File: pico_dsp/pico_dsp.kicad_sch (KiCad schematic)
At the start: 81 parts, among them J1 HDR_20, J2 HDR_20, J3 SJ3-35082B-TR, J4 SJ3-35082B-TR, J5 SJ3-35082B-TR, J7 SJ3-35082B-TR, SW1 RotaryEncoder_Switch, SW2 RotaryEncoder_Switch, U1 PCM5102A, U2 PCM1802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

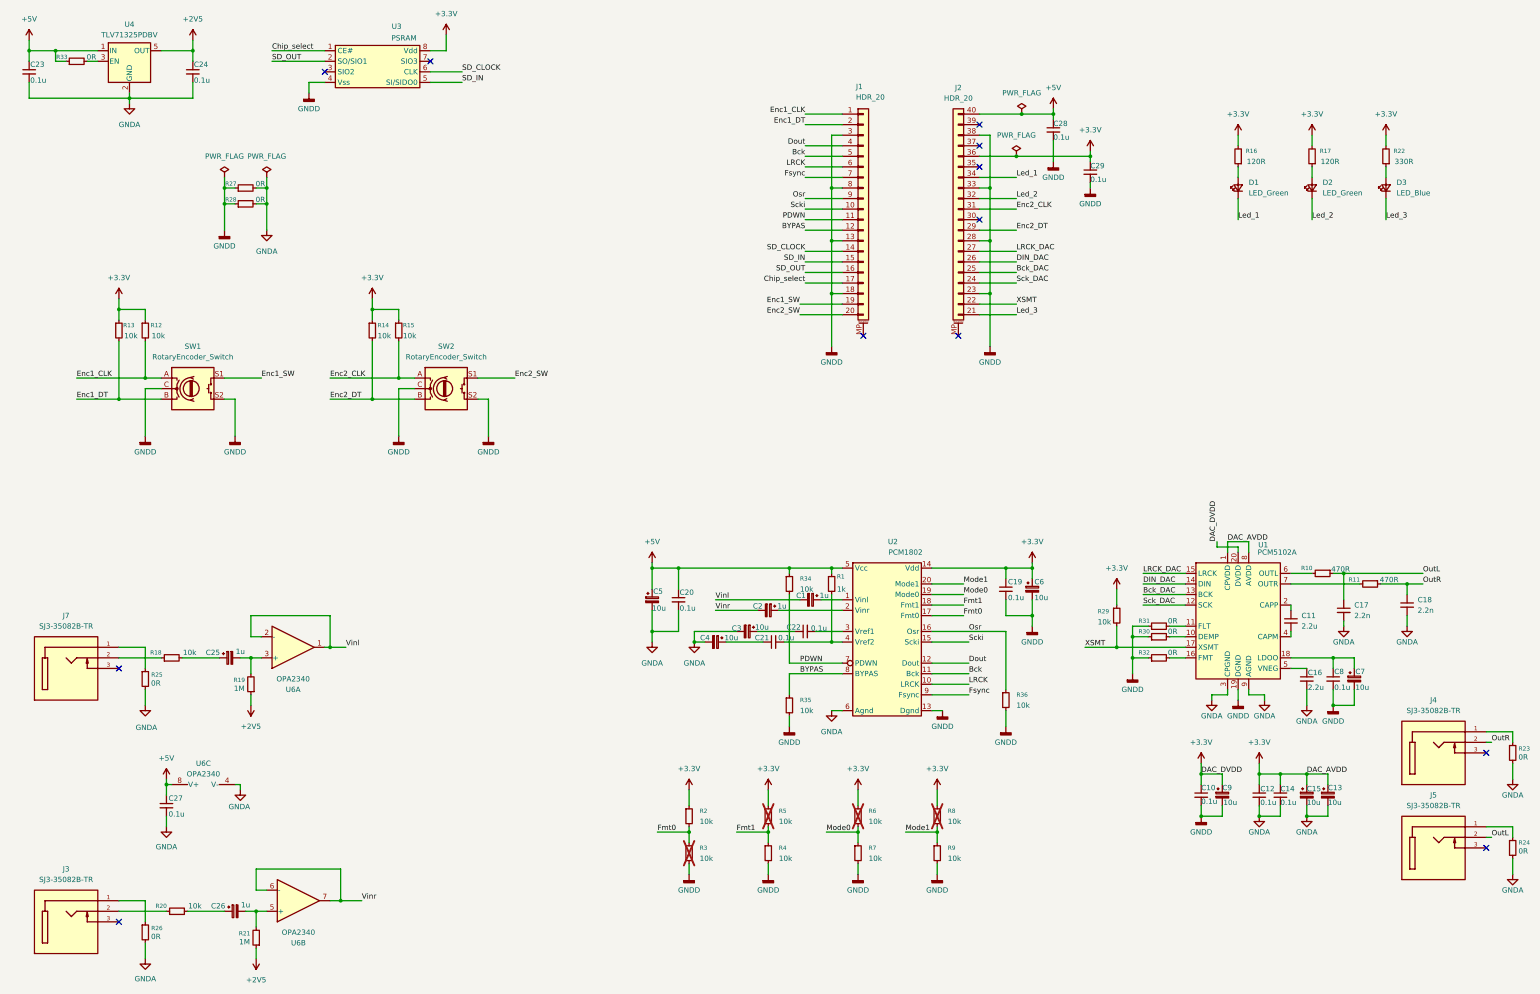
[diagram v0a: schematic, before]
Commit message: Added pads and updated pcb
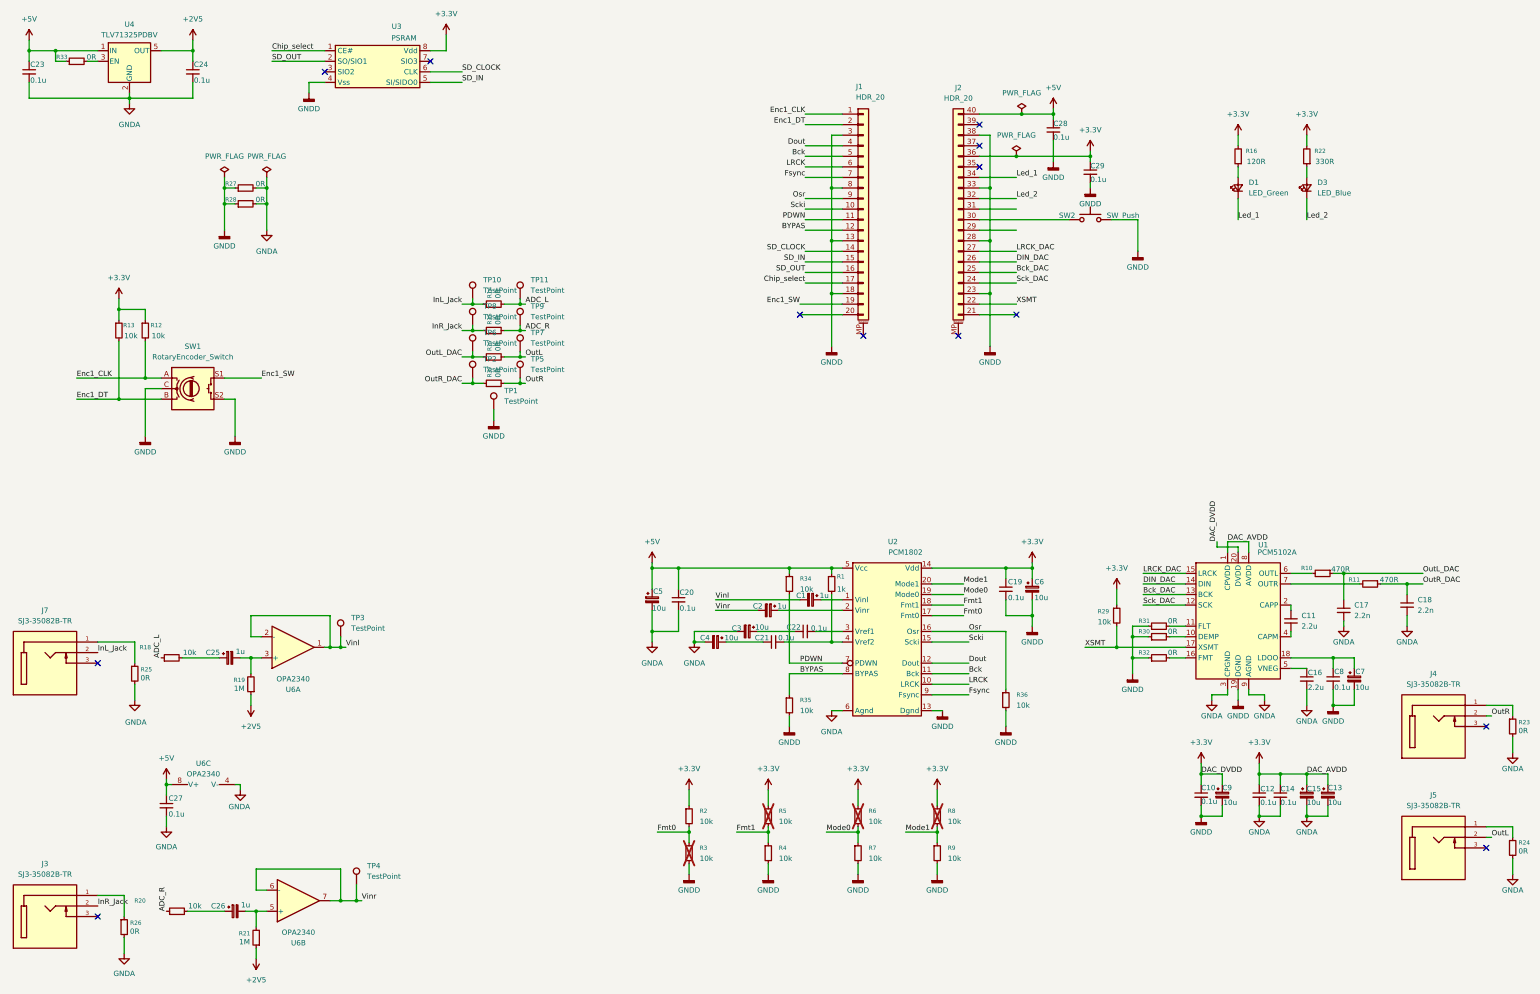
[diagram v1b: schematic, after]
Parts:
- removed D2: LED_Green, LED_SMD:LED_0603_1608Metric, symbol Device:LED_Small
- removed SW2: RotaryEncoder_Switch, Rotary_Encoder:RotaryEncoder_Bourns_Vertical_PEC12R-3x17F-Sxxxx, symbol Device:RotaryEncoder_Switch
- added R37: 0R, Resistor_SMD:R_0603_1608Metric, symbol Device:R_Small
- added SW2: SW_Push, Button_Switch_THT:SW_PUSH_6mm, symbol Switch:SW_Push
- added TP1, TP10, TP11, TP2, TP3, TP4, TP5, TP6, TP7, TP8, TP9: TestPoint, TestPoint:TestPoint_Pad_1.5x1.5mm, symbol Connector:TestPoint
- J3, J4, J5, J7: footprint SJ3-35082B-TR:SAMESKY_SJ3-35082B-TR -> Kicad-symbols:SAMESKY_SJ3-35082B-TR
- R14, R15: value 10k -> 0R
- R17: value 120R -> 0R
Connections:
- net +3.3V: no longer R14.1, R15.1, R17.2
- net GNDD: now also SW2.2, TP1.1
- net Led_2: now also D3.1 (K)
- net OutL: now also R17.2, TP7.1; no longer C17.1, R10.1
- net OutR: now also R37.2, TP5.1; no longer C18.1, R11.1
- net Vinl: now also TP3.1
- net Vinr: now also TP4.1
- net OutL_DAC: now reaches R17.1
- net OutL_DAC: now also C17.1, R10.1, TP6.1
- net at J2.30 (Pin_30): now also SW2.1
- net ADC_R: now reaches R20.1
- net ADC_R: now also R15.2, TP9.1; no longer J3.2
- net ADC_L: now reaches R18.1
- net ADC_L: now also R14.2, TP11.1; no longer J7.2
- net Enc2_CLK: no longer names the net of J2.31 (Pin_31)
- net Enc2_CLK: no longer R15.2
- net Enc2_DT: no longer names the net of J2.29 (Pin_29)
- net Enc2_DT: no longer R14.2
- net Enc2_SW: no longer names the net of J1.20 (Pin_20)
- net Led_3: no longer names the net of J2.21 (Pin_20)
- net Led_3: no longer D3.1 (K)
- new net InL_Jack: J7.2, R14.1, TP10.1
- new net InR_Jack: J3.2, R15.1, TP8.1
- new net OutR_DAC: C18.1, R11.1, R37.1, TP2.1
- no-connect marks 12 -> 13
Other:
- moved on the sheet: D3, J3, J4, J7, R22, R23, R25, R26
